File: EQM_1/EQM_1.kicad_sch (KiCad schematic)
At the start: 0 parts

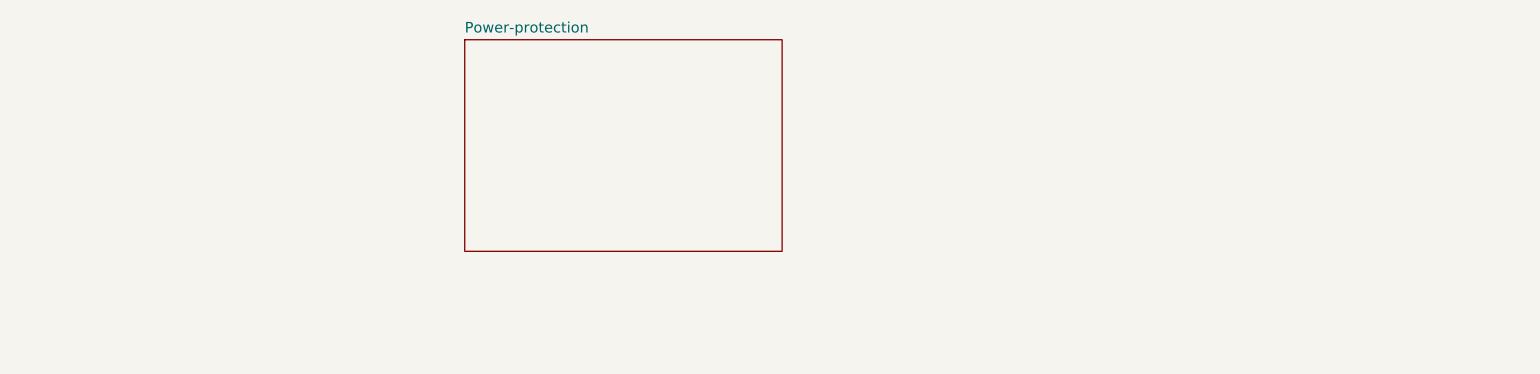
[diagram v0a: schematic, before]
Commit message: Temperatura
Se ha añadido el circuito del sensor de temperatura
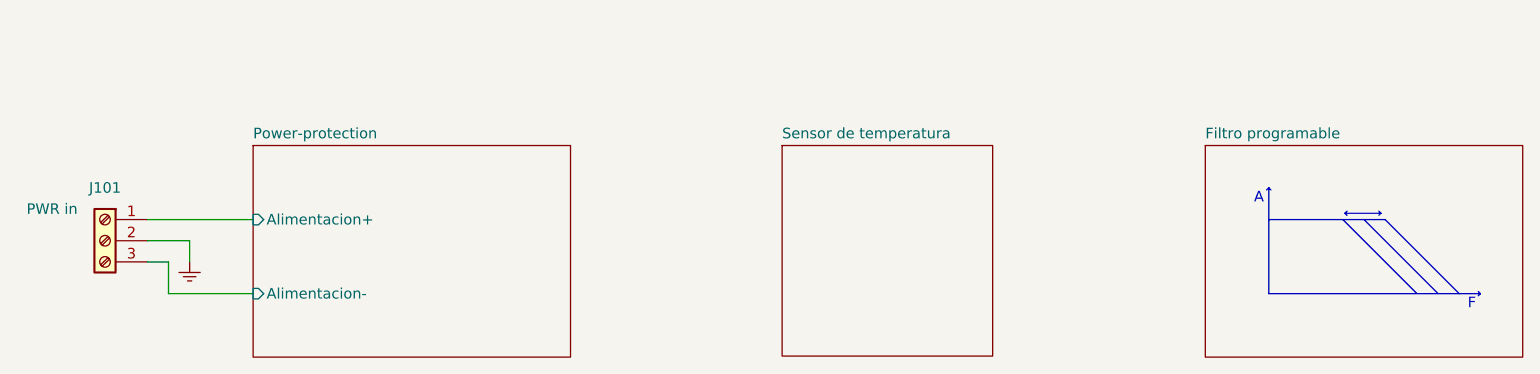
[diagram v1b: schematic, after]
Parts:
- added J101: Screw_Terminal_01x03, symbol Connector:Screw_Terminal_01x03
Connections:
- new net GND: J101.2 (Pin_2)
- new net Power-protection/Alimentacion+: J101.1 (Pin_1)
- new net Power-protection/Alimentacion-: J101.3 (Pin_3)
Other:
- added sheet Filtro programable (FP_sch.kicad_sch)
- added sheet Sensor de temperatura (ST_sch.kicad_sch)
- sheet Power-protection ports: added Alimentacion+, Alimentacion-; removed none
- note added: "A"
- note added: "F"

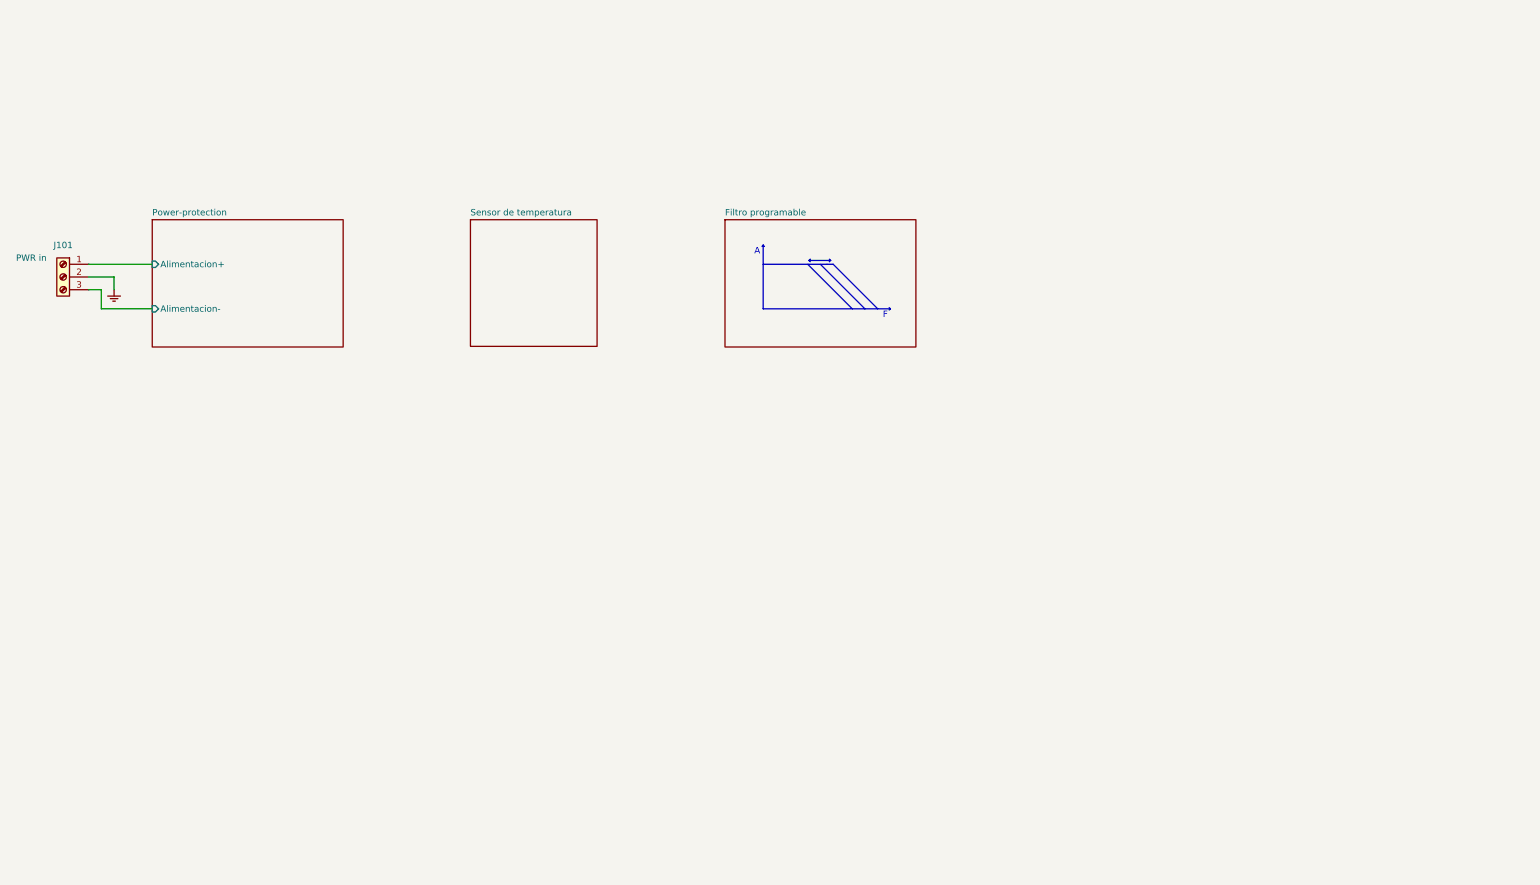
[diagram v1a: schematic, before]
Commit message: Esquema finalizado
El esquema está finalizado a falta de la asociación de footprints y la selección de valores para los pasivos
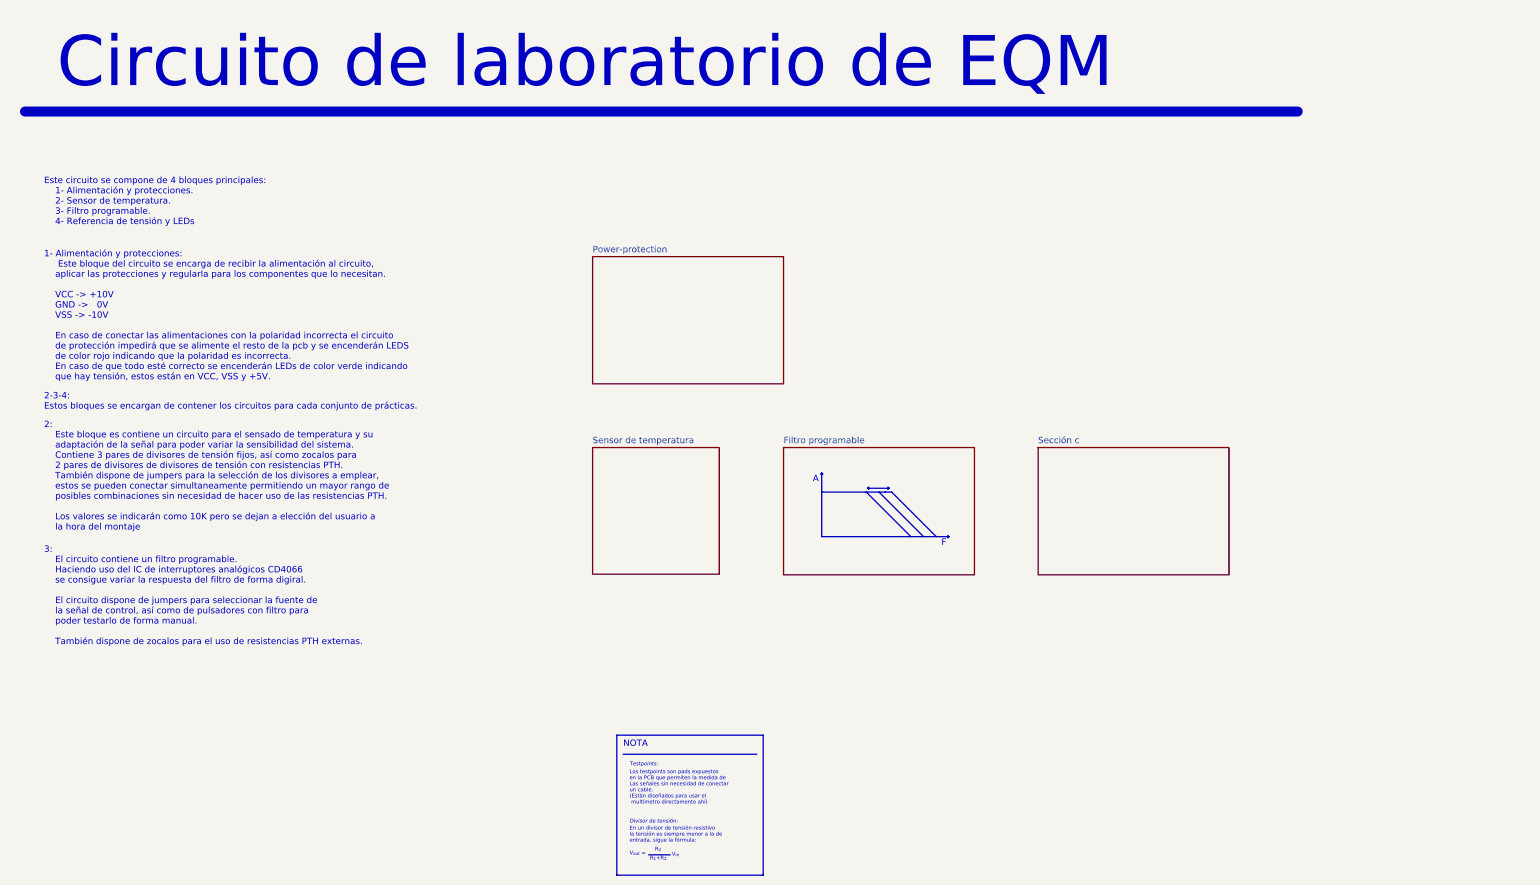
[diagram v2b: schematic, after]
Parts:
- removed J101: Screw_Terminal_01x03, symbol Connector:Screw_Terminal_01x03
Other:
- added sheet Sección c (secc_sch.kicad_sch)
- sheet Power-protection ports: added none; removed Alimentacion+, Alimentacion-
- note added: "1- Alimentación y protecciones: Este bloque del circuito se encarga de recibir la alimentación al circuito, aplicar las protecciones y regularla para los componentes que lo necesitan. VCC -> +10V GND -> 0V VSS -> -10V En caso de conectar las alimentaciones con la polaridad incorrecta el circuito de protección impedirá que se alimente el resto de la pcb y se encenderán LEDS de color rojo indicando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"
- note added: "2-3-4: Estos bloques se encargan de contener los circuitos para cada conjunto de prácticas."
- note added: "2: Este bloque es contiene un circuito para el sensado de temperatura y su adaptación de la señal para poder variar la sensibilidad del sistema. Contiene 3 pares de divisores de tensión fijos, así como zocalos para 2 pares de divisores de divisores de tensión con resistencias PTH. También dispone de jumpers para la selección de los divisores a emplear, estos se pueden conectar simultaneamente per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"
- note added: "3: El circuito contiene un filtro programable. Haciendo uso del IC de interruptores analógicos CD4066 se consigue variar la respuesta del filtro de forma digiral. El circuito dispone de jumpers para seleccionar la fuente de la señal de control, así como de pulsadores con filtro para poder testarlo de forma manual. También dispone de zocalos para el uso de resistencias PTH externas."
- note added: "Circuito de laboratorio de EQM"
- note added: "Divisor de tensión:"
- note added: "En un divisor de tensión resistivo la tensión es siempre menor a la de entrada, sigue la fórmula:"
- note added: "Este circuito se compone de 4 bloques principales: 1- Alimentación y protecciones. 2- Sensor de temperatura. 3- Filtro programable. 4- Referencia de tensión y LEDs"
- note added: "Los testpoints son pads expuestos en la PCB que permiten la medida de Las señales sin necesidad de conectar un cable. (Están diseñados para usar el multímetro directamente ahí)"
- note added: "NOTA"
- note added: "R_{1}+R_{2}"
- note added: "R_{2}"
- note added: "Testpoints:"
- note added: "V_{in}"
- note added: "V_{out} ="

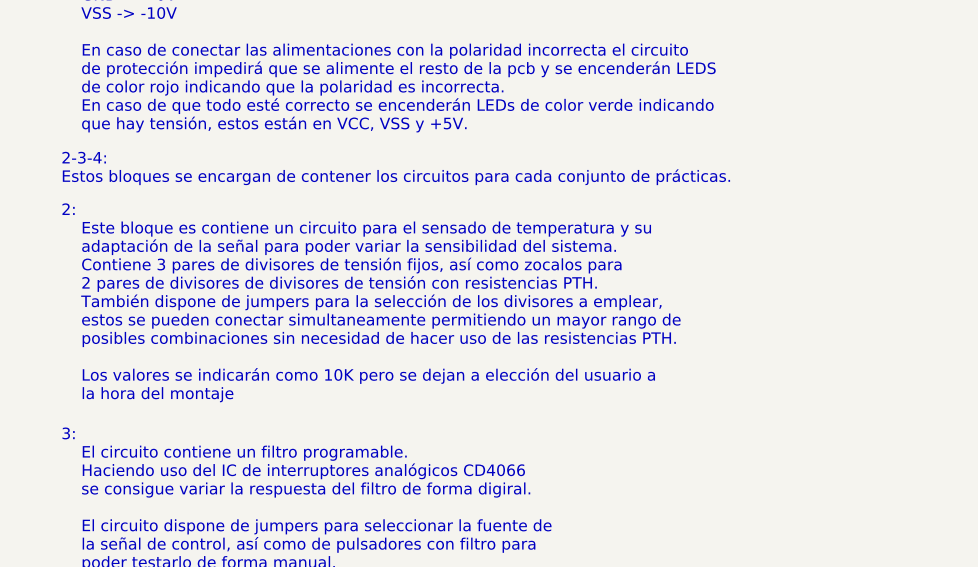
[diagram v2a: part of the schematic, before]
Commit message: PCB-1
Primer posicionamiento de los componentes en la pcb y ligeros cambios en el esquemático.
Posicionamiento MUY BASTO, simplemente para ver que los componentes caben en las dimensiones de la pcb elegida.
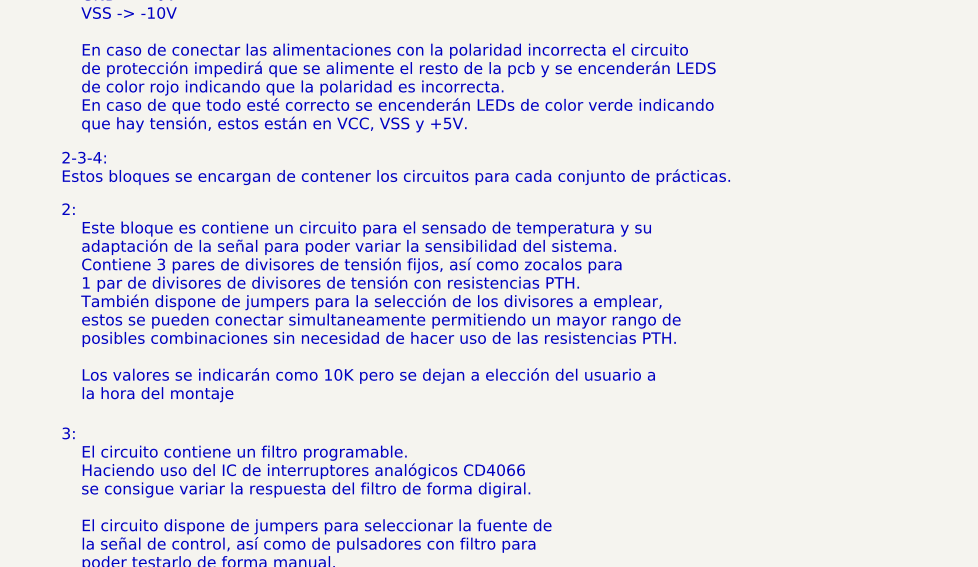
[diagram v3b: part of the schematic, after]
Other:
- note added: "2: Este bloque es contiene un circuito para el sensado de temperatura y su adaptación de la señal para poder variar la sensibilidad del sistema. Contiene 3 pares de divisores de tensión fijos, así como zocalos para 1 par de divisores de divisores de tensión con resistencias PTH. También dispone de jumpers para la selección de los divisores a emplear, estos se pueden conectar simultaneamente permi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"
- note removed: "2: Este bloque es contiene un circuito para el sensado de temperatura y su adaptación de la señal para poder variar la sensibilidad del sistema. Contiene 3 pares de divisores de tensión fijos, así como zocalos para 2 pares de divisores de divisores de tensión con resistencias PTH. También dispone de jumpers para la selección de los divisores a emplear, estos se pueden conectar simultaneamente per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"
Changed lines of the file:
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@@
     (effects (font (size 0.75 0.75)) (justify left bottom))
   )
-  (text "2:\n	Este bloque es contiene un circuito para el sensado de temperatura y su\n	adaptación de la señal para poder variar la sensibilidad del sistema.\n	Contiene 3 pares de divisores de tensión fijos, así como zocalos para \n	2 pares de divisores de divisores de tensión con resistencias PTH.\n	También dispone de jumpers para la selección de los divisores a emplear,\n	estos se pueden conectar simultaneamente permitiendo un mayor rango de \n	posibles combinaciones sin necesidad de hacer uso de las resistencias PTH.\n\n	Los valores se indicarán como 10K pero se dejan a elección del usuario a \n	la hora del montaje"
+  (text "2:\n	Este bloque es contiene un circuito para el sensado de temperatura y su\n	adaptación de la señal para poder variar la sensibilidad del sistema.\n	Contiene 3 pares de divisores de tensión fijos, así como zocalos para \n	1 par de divisores de divisores de tensión con resistencias PTH.\n	También dispone de jumpers para la selección de los divisores a emplear,\n	estos se pueden conectar simultaneamente permitiendo un mayor rango de \n	posibles combinaciones sin necesidad de hacer uso de las resistencias PTH.\n\n	Los valores se indicarán como 10K pero se dejan a elección del usuario a \n	la hora del montaje"
     (at 29.21 125.73 0)
     (effects (font (size 1.27 1.27)) (justify left bottom))
